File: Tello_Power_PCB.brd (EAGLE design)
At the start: 122.5 x 89.3 mm, 122 parts, among them CON1 XT30PW-F, CON2 XT30PW-F, CON3 XT30PW-F, CON4 XT30PW-F, CON7 XT60PW-M, J1 PJ-002A, J10 SM02BGHSTBLFSN, J2 1719740002, J3 1719740002, J4 1719740002, J5 1719740002, J6 1719740002, J7 1719740002, J8 1719740002, J9 1719740002, M1 30V, M2 60V, M3 30V, M4 60V, Q1 BSC027N06LS5ATMA1, Q2 BSC027N06LS5ATMA1, Q3 IXTA96P085T, Q7 IXTA96P085T, Q8 IXTA96P085T, Q9 IXTA96P085T, U1 LM3150MH/NOPB, U10 TLV6713DDCTDDC0006A_M, U11 TLV7041DCKR, U12 DMN67D8LW-13, U13 MCP1792T-5002H/CB, U2 LM3150MH/NOPB, U3 LTC4357CMS8TRPBF, U4 ADS1015IDGST, U6 DMN67D8LW-13, U7 DMN67D8LW-13, U8 LTC4357CMS8TRPBF, U9 TLV6713DDCTDDC0006A_M

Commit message: Finished Routing PCB, Needs Design Review
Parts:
- removed R30: 1.62K, rcl:R0603
- removed U11: TLV7041DCKR, TLV7041DCKR:SOT65P210X110-5N
- removed U12: DMN67D8LW-13, DMN67D8LW-13:DMN67D8LW-13_DIO
- added LED4: (no value), led:CHIP-LED0603
- added R36: 10K, microbuilder:0603
- added R37: 1K, microbuilder:0603
- R19: value 10K -> 1K
- R22: value 10K -> 5K
- R25: value (none) -> 2K
- R29: value 1.8K -> 2K
- moved R29 184.3 mm to (-2.51, 26.3), turned to 90 degrees
- moved R19 179.7 mm to (-5.50, 26.3), turned to 90 degrees
- moved R22 145.6 mm to (-22.8, 0.31)
- moved R25 132.7 mm to (-6.50, 15.0), turned to 90 degrees
- moved U9 117.9 mm to (15.1, -49.9)
- moved R21 111.1 mm to (21.3, -48.9)
- moved U10 68.0 mm to (26.5, -34.0), turned to 270 degrees
- moved R20 64.5 mm to (27.6, -30.4)
- moved LED3 5.02 mm to (-7.16, 33.7)
- moved LED2 3.54 mm to (-11.6, 33.7)
- moved LED1 2.27 mm to (-16.3, 33.8), turned to 270 degrees
- moved R13 1.14 mm to (27.5, -27.8)
- moved R5 0.74 mm to (27.5, -21.0)
- moved R12 0.71 mm to (27.6, -26.1)
- moved U7 0.64 mm to (27.6, -23.4)
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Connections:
- removed net N$3: R19.1, R29.2, U11.IN+
- removed net N_GATE: R14.1, R16.1, U6.1
- removed net N_GATE_M: R12.1, R13.1, U7.1
- removed net PS_SV_COMP: R25.1, U11.OUT, U12.1
- removed net ROBOT_V+: C17.1, C18.1, C19.1, C4.1, C5.1, C6.1
- removed net SYS_UV_SOURCE: U12.2, U9.OUT
- new net N$31: R36.2, R37.1, U4.7
- new net N$32: LED3.A, R25.2
- new net N$33: LED2.A, R22.2
- new net N$34: LED1.A, R19.2
- net 5V: now also R19.1
- net 5V_ALWAYS_ON: no longer R25.2
- net BATT_IN: no longer R21.2, R22.2
- net GND: now also LED1.C, LED2.C, LED3.C, LED4.C, R37.2; no longer R29.1, R30.1
- net MOTOR_V+: now also R29.1, R36.1
- net M_N_GATE: now also R12.1, R13.1, U7.1
- net N$6: now also LED4.A, R29.2; no longer R22.1, R30.2, U11.IN-
- net PS_IN: no longer R19.2
- net SYSTEM_IN: now also R21.2, R25.1
- net SYSTEM_SWITCHED: now also C17.1, C18.1, C19.1, C4.1, C5.1, C6.1
- net S_N_GATE: now also R14.1, R16.1, U6.1, U9.OUT; no longer U12.3
- net V_ADJ: now also R22.1
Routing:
- net MOTOR_V+: track 18.2 -> 128.8 mm, vias 1 -> 3
- net 5V_ALWAYS_ON: track 28.2 -> 112.6 mm, vias 0 -> 3
- net 5V: track 64.1 -> 144.6 mm, vias 0 -> 3
- net N$8: track 0.00 -> 68.7 mm, vias 0 -> 2
- net N$9: track 0.00 -> 60.1 mm, vias 0 -> 2
- net N$33: track 0.00 -> 38.4 mm, vias 0 -> 1
- net P_GATES_MOTOR: track 8.84 -> 44.8 mm
- net N$34: track 0.00 -> 22.8 mm, vias 0 -> 1
- net V_ADJ: track 89.7 -> 109.5 mm
- net N$32: track 0.00 -> 18.7 mm, vias 0 -> 1
- net GND: track 13.2 -> 31.1 mm, vias 148 -> 389
- net N$31: track 0.00 -> 16.3 mm, vias 0 -> 2
- net S_N_GATE: track 0.00 -> 10.7 mm
- net M_N_GATE: track 0.00 -> 8.67 mm
- net N_GATE: track 7.48 -> 0.00 mm
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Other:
- board text added: "Features: - Adj. System Under Voltage Protection - Adj. Motor Under Voltage Protection - 5v Regulated Output - Adj. Regulated Output - Hot Swapping between Battery & Power Supply - I2C ADC Voltage Sensing: - Battery Voltage - Power Supply Voltage - Motor Voltage - Adj. Reg. Voltage - Expansion Ports: - Additional XT30 Motor Ports - Additional Regulated Power Ports"
- board text added: "Mtrs"
- board text added: "Sys."
- board text added: "V+"
- board text removed: "Batt"
- board text removed: "EDIT PS_IN DIODE FOOTPRINT"
- board text removed: "NEED: Low Battery cuttoff 5V ALAWAYS ON Reg - ?"

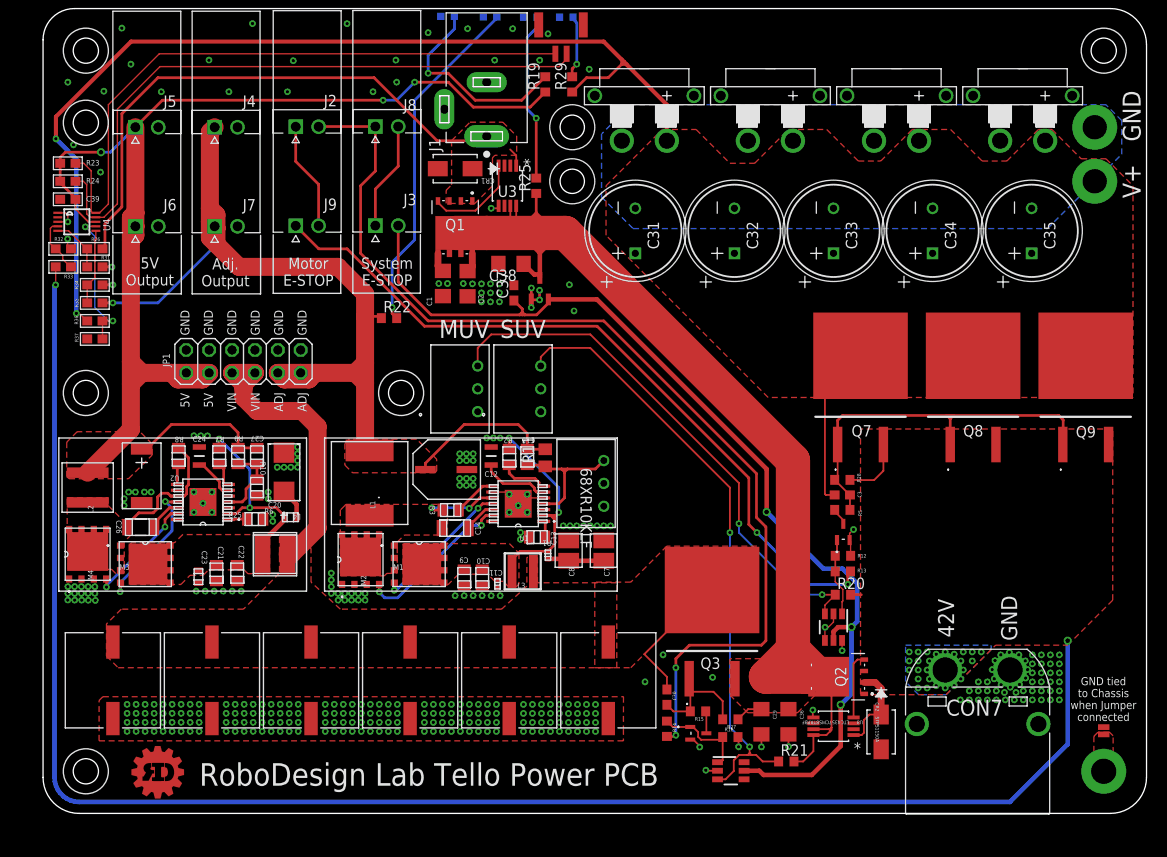
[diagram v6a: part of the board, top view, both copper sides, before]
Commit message: added UV 30s delay circuit
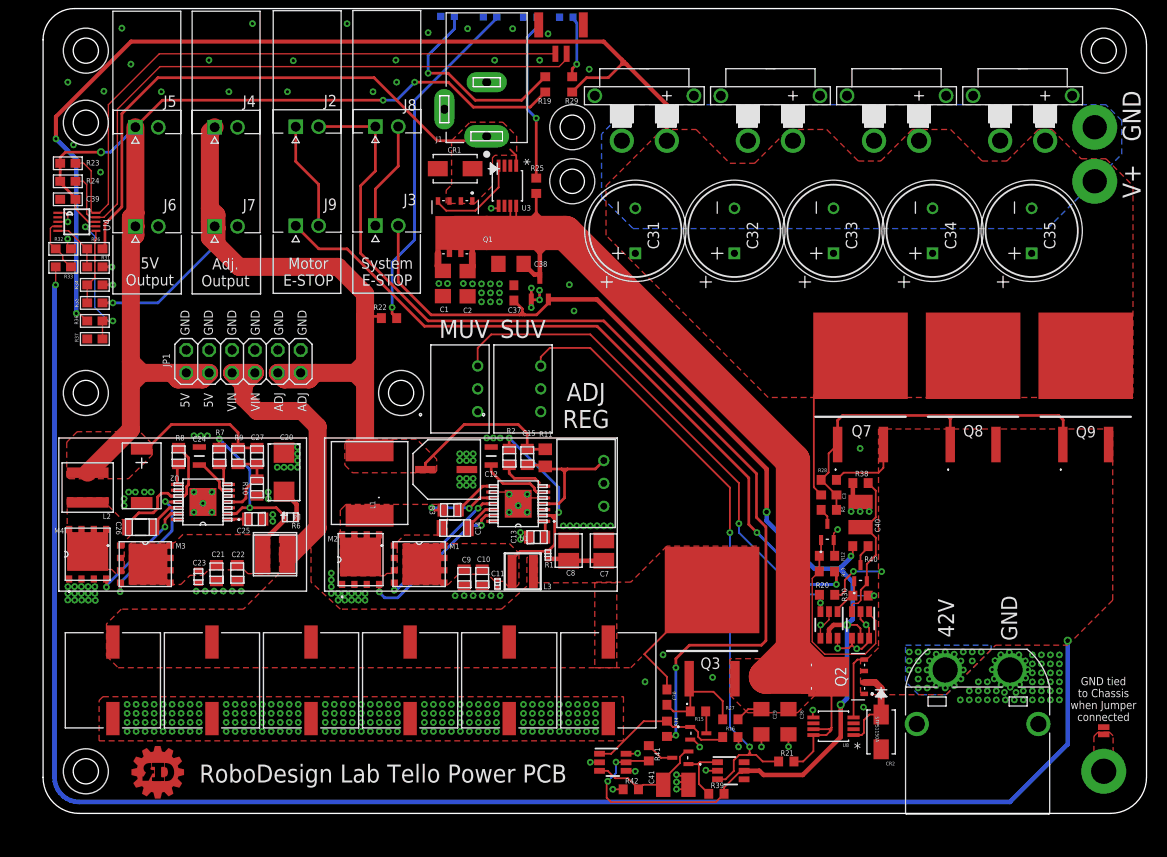
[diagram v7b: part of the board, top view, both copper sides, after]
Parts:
- added C40, C41: 220uF, rcl:C1210
- added R30, R39: 1K, rcl:R0603
- added R38, R42: 62K, rcl:R0603
- added R40, R41: 100R, rcl:R0603
- added U11, U14: TLV6713DDCTDDC0006A_M, TLV6713DDC:DDC0006A_M
- added U12, U5: DMN67D8LW-13, DMN67D8LW-13:DMN67D8LW-13_DIO
- moved R12 1.77 mm to (25.8, -26.1)
- moved R13 1.77 mm to (25.8, -27.8)
- moved U7 1.77 mm to (25.8, -23.4)
- moved R20 1.76 mm to (25.8, -30.4)
- moved C3 1.50 mm to (26.0, -19.3)
- moved R28 1.50 mm to (26.0, -17.6)
- moved R5 1.50 mm to (26.0, -21.0)
- moved U10 0.56 mm to (26.0, -33.8)
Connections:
- new net N$3: R30.1, U10.OUT, U5.1
- new net N$35: C40.1, R38.2, U11.SENSE, U5.2
- new net N$36: R40.1, U5.3
- new net N$37: R39.1, U12.1, U9.OUT
- new net N$38: R41.1, U12.3
- new net N$39: C41.1, R42.2, U12.2, U14.SENSE
- net 5V_ALWAYS_ON: now also R30.2, R39.2, R40.2, R41.2, U11.VCC, U14.VCC
- net GND: now also C40.2, C41.2, R38.1, R42.1, U11.GND, U11.GND@1, U11.GND@2, U14.GND, U14.GND@1, U14.GND@2
- net M_N_GATE: now also U11.OUT; no longer U10.OUT
- net S_N_GATE: now also U14.OUT; no longer U9.OUT
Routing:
- net 5V_ALWAYS_ON: track 112.6 -> 147.5 mm, vias 3 -> 7
- net GND: track 31.1 -> 53.8 mm, vias 389 -> 403
- net N$35: track 0.00 -> 17.6 mm
- net M_N_GATE: track 8.67 -> 23.7 mm
- net N$39: track 0.00 -> 13.2 mm
- net N$37: track 0.00 -> 7.31 mm
- net BATT_IN: track 203.1 -> 210.2 mm, vias 28 -> 30
- net S_N_GATE: track 10.7 -> 16.5 mm
- net N$3: track 0.00 -> 4.26 mm
- net N$38: track 0.00 -> 3.16 mm
- net N$36: track 0.00 -> 2.45 mm
- net N$9: track 60.1 -> 58.4 mm
- net MOTOR_PULLUP: track 82.4 -> 81.2 mm
- net P_GATES_MOTOR: track 44.8 -> 45.4 mm
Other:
- board text added: "ADJ REG"

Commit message: Organized Schematic, Ready for Detailed Review
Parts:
- C7, C8: value 4.7uF -> 2.2uF
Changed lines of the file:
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@@
 <attribute name="VENDOR" value="Panasonic" x="-37.5" y="2.9" size="1.778" layer="27" rot="R270" display="off"/>
 </element>
-<element name="C8" library="12v- LM3150" library_urn="urn:adsk.eagle:library:14070849" package="3528-21" package3d_urn="urn:adsk.eagle:package:14070891/1" value="4.7uF" x="-2.9" y="-25.5" smashed="yes" rot="R90">
+<element name="C8" library="12v- LM3150" library_urn="urn:adsk.eagle:library:14070849" package="3528-21" package3d_urn="urn:adsk.eagle:package:14070891/1" value="2.2uF" x="-2.9" y="-25.5" smashed="yes" rot="R90">
 <attribute name="CAP" value="4.7E6" x="36.1" y="-46.5" size="1.778" layer="27" rot="R90" display="off"/>
 <attribute name="ESR" value="0.7" x="36.1" y="-46.5" size="1.778" layer="27" rot="R90" display="off"/>
@@
 <attribute name="RS_PRICE-STOCK" value="" x="0" y="25.2" size="1.778" layer="27" rot="R180" display="off"/>
 </element>
-<element name="C7" library="12v- LM3150" library_urn="urn:adsk.eagle:library:14070849" package="3528-21" package3d_urn="urn:adsk.eagle:package:14070891/1" value="4.7uF" x="1" y="-25.5" smashed="yes" rot="R90">
+<element name="C7" library="12v- LM3150" library_urn="urn:adsk.eagle:library:14070849" package="3528-21" package3d_urn="urn:adsk.eagle:package:14070891/1" value="2.2uF" x="1" y="-25.5" smashed="yes" rot="R90">
 <attribute name="CAP" value="4.7E6" x="70" y="-40.5" size="1.778" layer="27" rot="R90" display="off"/>
 <attribute name="ESR" value="0.7" x="70" y="-40.5" size="1.778" layer="27" rot="R90" display="off"/>
